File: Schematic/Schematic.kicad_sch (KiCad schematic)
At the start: 12 parts, among them J7 USB_C_Receptacle_PowerOnly_6P, U1 L7805, U2 MCP1700x-330xxTO

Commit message: Fix USB sheild connection
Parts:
- R38, R39: footprint Resistor_THT:R_Axial_DIN0204_L3.6mm_D1.6mm_P5.08mm_Vertical -> Resistor_SMD:R_1812_4532Metric_Pad1.30x3.40mm_HandSolder
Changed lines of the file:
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@@
+	)
+	(junction
+		(at 73.66 82.55)
+		(diameter 0)
+		(color 0 0 0 0)
 	)
 	(junction
@@
 		(color 0 0 0 0)
 	)
-	(junction
-		(at 73.66 82.55)
-		(diameter 0)
-		(color 0 0 0 0)
-	)
 	(wire
 		(pts
@@
 	(wire
 		(pts
+			(xy 41.91 154.94) (xy 41.91 156.21)
+		)
+		(stroke
+			(width 0)
+			(type default)
+		)
+	)
+	(wire
+		(pts
 			(xy 58.42 40.64) (xy 58.42 44.45)
 		)
@@
 	(wire
 		(pts
-			(xy 34.29 154.94) (xy 34.29 153.67)
-		)
-		(stroke
-			(width 0)
-			(type default)
-		)
-	)
-	(wire
-		(pts
 			(xy 71.12 40.64) (xy 91.44 40.64)
 		)
@@
 	(wire
 		(pts
+			(xy 34.29 154.94) (xy 41.91 154.94)
+		)
+		(stroke
+			(width 0)
+			(type default)
+		)
+	)
+	(wire
+		(pts
 			(xy 41.91 90.17) (xy 57.15 90.17)
 		)
@@
 	(wire
 		(pts
-			(xy 34.29 154.94) (xy 41.91 154.94)
+			(xy 34.29 153.67) (xy 34.29 154.94)
 		)
 		(stroke
@@
 	(wire
 		(pts
-			(xy 41.91 154.94) (xy 41.91 156.21)
+			(xy 41.91 153.67) (xy 41.91 154.94)
 		)
 		(stroke
@@
 		(pts
 			(xy 22.86 33.02) (xy 29.21 33.02)
-		)
-		(stroke
-			(width 0)
-			(type default)
-		)
-	)
-	(wire
-		(pts
-			(xy 41.91 154.94) (xy 41.91 153.67)
 		)
 		(stroke
@@
 			)
 		)
-		(property "Footprint" "Resistor_THT:R_Axial_DIN0204_L3.6mm_D1.6mm_P5.08mm_Vertical"
+		(property "Footprint" "Resistor_SMD:R_1812_4532Metric_Pad1.30x3.40mm_HandSolder"
 			(at 70.358 148.59 90)
 			(effects
@@
 			)
 		)
-		(property "Footprint" "Resistor_THT:R_Axial_DIN0204_L3.6mm_D1.6mm_P5.08mm_Vertical"
+		(property "Footprint" "Resistor_SMD:R_1812_4532Metric_Pad1.30x3.40mm_HandSolder"
 			(at 81.788 148.59 90)
 			(effects

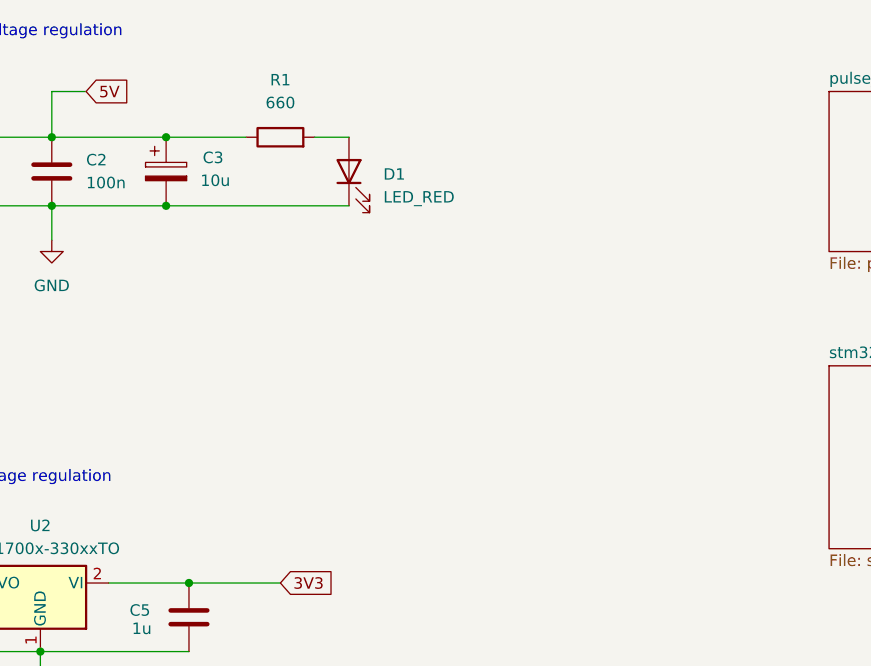
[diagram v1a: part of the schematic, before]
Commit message: fix schematic and pcb layout
Fix Potentiometer errors, and updated schematic
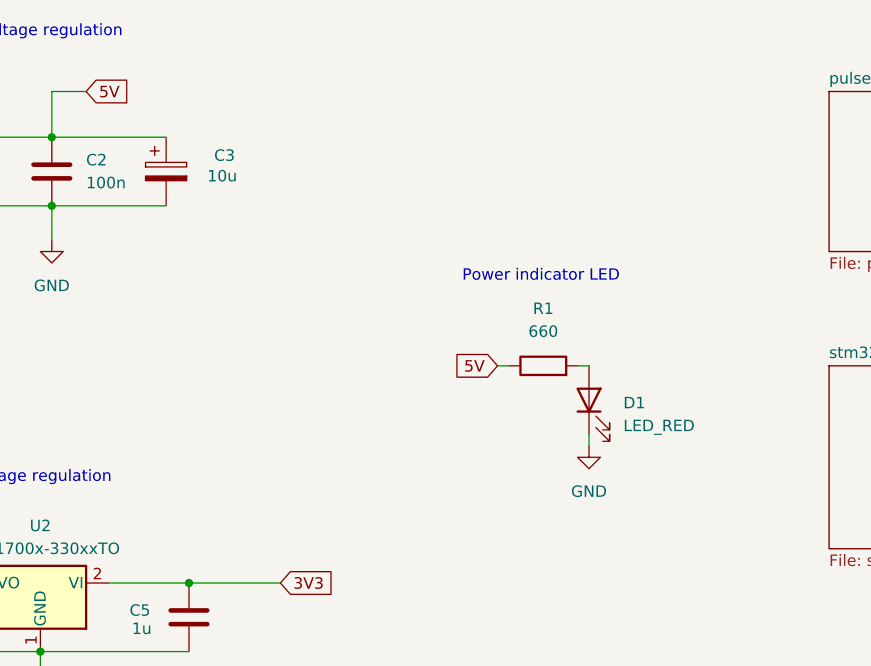
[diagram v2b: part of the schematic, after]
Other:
- note added: "Power indicator LED"
- moved on the sheet: D1, R1
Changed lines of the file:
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@@
 	(generator_version "9.0")
 	(paper "A4")
+	(text "Power indicator LED\n"
+		(exclude_from_sim no)
+		(at 112.776 48.514 0)
+		(effects
+			(font
+				(size 1.27 1.27)
+			)
+		)
+	)
 	(text "3V3 voltage regulation"
 		(exclude_from_sim no)
@@
 	)
 	(junction
-		(at 71.12 33.02)
-		(diameter 0)
-		(color 0 0 0 0)
-	)
-	(junction
-		(at 71.12 40.64)
-		(diameter 0)
-		(color 0 0 0 0)
-	)
-	(junction
 		(at 58.42 33.02)
 		(diameter 0)
@@
 	(wire
 		(pts
+			(xy 107.95 58.42) (xy 109.22 58.42)
+		)
+		(stroke
+			(width 0)
+			(type default)
+		)
+	)
+	(wire
+		(pts
 			(xy 64.77 82.55) (xy 73.66 82.55)
 		)
@@
 	(wire
 		(pts
-			(xy 71.12 33.02) (xy 80.01 33.02)
-		)
-		(stroke
-			(width 0)
-			(type default)
-		)
-	)
-	(wire
-		(pts
 			(xy 41.91 82.55) (xy 49.53 82.55)
 		)
@@
 	(wire
 		(pts
-			(xy 87.63 33.02) (xy 91.44 33.02)
-		)
-		(stroke
-			(width 0)
-			(type default)
-		)
-	)
-	(wire
-		(pts
-			(xy 71.12 40.64) (xy 91.44 40.64)
+			(xy 116.84 58.42) (xy 118.11 58.42)
 		)
 		(stroke
@@
 		(pts
 			(xy 34.29 153.67) (xy 34.29 154.94)
+		)
+		(stroke
+			(width 0)
+			(type default)
+		)
+	)
+	(wire
+		(pts
+			(xy 118.11 66.04) (xy 118.11 67.31)
 		)
 		(stroke
@@
 				)
 				(justify left)
+				(hide yes)
+			)
+		)
+	)
+	(global_label "5V"
+		(shape input)
+		(at 107.95 58.42 180)
+		(fields_autoplaced yes)
+		(effects
+			(font
+				(size 1.27 1.27)
+			)
+			(justify right)
+		)
+		(property "Intersheetrefs" "${INTERSHEET_REFS}"
+			(at 102.6667 58.42 0)
+			(effects
+				(font
+					(size 1.27 1.27)
+				)
+				(justify right)
 				(hide yes)
 			)
@@
 	)
 	(symbol
+		(lib_id "power:GND")
+		(at 118.11 67.31 0)
+		(unit 1)
+		(exclude_from_sim no)
+		(in_bom yes)
+		(on_board yes)
+		(dnp no)
+		(fields_autoplaced yes)
+		(property "Reference" "#PWR030"
+			(at 118.11 73.66 0)
+			(effects
+				(font
+					(size 1.27 1.27)
+				)
+				(hide yes)
+			)
+		)
+		(property "Value" "GND"
+			(at 118.11 72.39 0)
+			(effects
+				(font
+					(size 1.27 1.27)
+				)
+			)
+		)
+		(property "Footprint" ""
+			(at 118.11 67.31 0)
+			(effects
+				(font
+					(size 1.27 1.27)
+				)
+				(hide yes)
+			)
+		)
+		(property "Datasheet" ""
+			(at 118.11 67.31 0)
+			(effects
+				(font
+					(size 1.27 1.27)
+				)
+				(hide yes)
+			)
+		)
+		(property "Description" "Power symbol creates a global label with name \"GND\" , ground"
+			(at 118.11 67.31 0)
+			(effects
+				(font
+					(size 1.27 1.27)
+				)
+				(hide yes)
+			)
+		)
+		(pin "1"
+		)
+		(instances
+			(project "Schematic"
+				(path "/e489aebc-5c18-43ce-b37f-71b1d4c7067c"
+					(reference "#PWR030")
+					(unit 1)
+				)
+			)
+		)
+	)
+	(symbol
 		(lib_id "Device:C")
 		(at 58.42 36.83 0)
@@
 		(dnp no)
 		(property "Reference" "C3"
-			(at 75.184 35.306 0)
+			(at 76.454 35.052 0)
 			(effects
 				(font
@@
 		)
 		(property "Value" "10u"
-			(at 74.93 37.846 0)
+			(at 75.692 37.338 0)
 			(effects
 				(font
@@
 	(symbol
 		(lib_id "Device:R")
-		(at 83.82 33.02 90)
+		(at 113.03 58.42 90)
 		(unit 1)
 		(exclude_from_sim no)
@@
 		(fields_autoplaced yes)
 		(property "Reference" "R1"
-			(at 83.82 26.67 90)
+			(at 113.03 52.07 90)
 			(effects
 				(font
@@
 		)
 		(property "Value" "660"
-			(at 83.82 29.21 90)
+			(at 113.03 54.61 90)
 			(effects
 				(font
@@
 		)
 		(property "Footprint" "Resistor_THT:R_Axial_DIN0204_L3.6mm_D1.6mm_P5.08mm_Vertical"
-			(at 83.82 34.798 90)
+			(at 113.03 60.198 90)
 			(effects
 				(font
@@
 		)
 		(property "Datasheet" "~"
-			(at 83.82 33.02 0)
+			(at 113.03 58.42 0)
 			(effects
 				(font
@@
 		)
 		(property "Description" "Resistor"
-			(at 83.82 33.02 0)
+			(at 113.03 58.42 0)
 			(effects
 				(font
@@
 	(symbol
 		(lib_id "Device:LED")
-		(at 91.44 36.83 90)
+		(at 118.11 62.23 90)
 		(unit 1)
 		(exclude_from_sim no)
@@
 		(fields_autoplaced yes)
 		(property "Reference" "D1"
-			(at 95.25 37.1474 90)
+			(at 121.92 62.5474 90)
 			(effects
 				(font
@@
 		)
 		(property "Value" "LED_RED"
-			(at 95.25 39.6874 90)
+			(at 121.92 65.0874 90)
 			(effects
 				(font
@@
 		)
 		(property "Footprint" "LED_THT:LED_D8.0mm"
-			(at 91.44 36.83 0)
+			(at 118.11 62.23 0)
 			(effects
 				(font
@@
 		)
 		(property "Datasheet" "~"
-			(at 91.44 36.83 0)
+			(at 118.11 62.23 0)
 			(effects
 				(font
@@
 		)
 		(property "Description" "Light emitting diode"
-			(at 91.44 36.83 0)
+			(at 118.11 62.23 0)
 			(effects
 				(font
@@
 		)
 		(property "Sim.Pins" "1=K 2=A"
-			(at 91.44 36.83 0)
-			(effects
-				(font
+			(at 118.11 62.23 0)
+			(effects
+				(font

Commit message: update
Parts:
- D1: footprint LED_THT:LED_D8.0mm -> LED_THT:LED_D3.0mm_Horizontal_O3.81mm_Z2.0mm
- R1: footprint Resistor_THT:R_Axial_DIN0204_L3.6mm_D1.6mm_P5.08mm_Vertical -> Resistor_THT:R_Axial_DIN0309_L9.0mm_D3.2mm_P12.70mm_Horizontal
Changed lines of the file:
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@@
 			)
 		)
-		(property "Footprint" "Resistor_THT:R_Axial_DIN0204_L3.6mm_D1.6mm_P5.08mm_Vertical"
+		(property "Footprint" "Resistor_THT:R_Axial_DIN0309_L9.0mm_D3.2mm_P12.70mm_Horizontal"
 			(at 113.03 60.198 90)
 			(effects
@@
 			)
 		)
-		(property "Footprint" "LED_THT:LED_D8.0mm"
+		(property "Footprint" "LED_THT:LED_D3.0mm_Horizontal_O3.81mm_Z2.0mm"
 			(at 118.11 62.23 0)
 			(effects

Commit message: Update PCB
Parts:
- J7: footprint Connector_USB:USB_C_Receptacle_GCT_USB4125-xx-x-0190_6P_TopMnt_Horizontal -> Connector_USB:USB_C_Receptacle_GCT_USB4125-xx-x_6P_TopMnt_Horizontal
- U2: footprint Package_TO_SOT_THT:TO-92_Inline -> Package_TO_SOT_THT:TO-92_Inline_Wide
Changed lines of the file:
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@@
 			)
 		)
-		(property "Footprint" "Connector_USB:USB_C_Receptacle_GCT_USB4125-xx-x-0190_6P_TopMnt_Horizontal"
+		(property "Footprint" "Connector_USB:USB_C_Receptacle_GCT_USB4125-xx-x_6P_TopMnt_Horizontal"
 			(at 45.72 133.35 0)
 			(effects
@@
 			)
 		)
-		(property "Footprint" "Package_TO_SOT_THT:TO-92_Inline"
+		(property "Footprint" "Package_TO_SOT_THT:TO-92_Inline_Wide"
 			(at 57.15 77.47 0)
 			(effects
